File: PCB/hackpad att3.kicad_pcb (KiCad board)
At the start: 2 copper layers, 99 x 41 mm, 12 parts, among them SW1 SW_Push, SW2 SW_Push, SW3 SW_Push, SW4 SW_Push, SW5 SW_Push, SW6 SW_Push, SW9 RotaryEncoder_Switch, U1 XIAO-RP2040-DIP

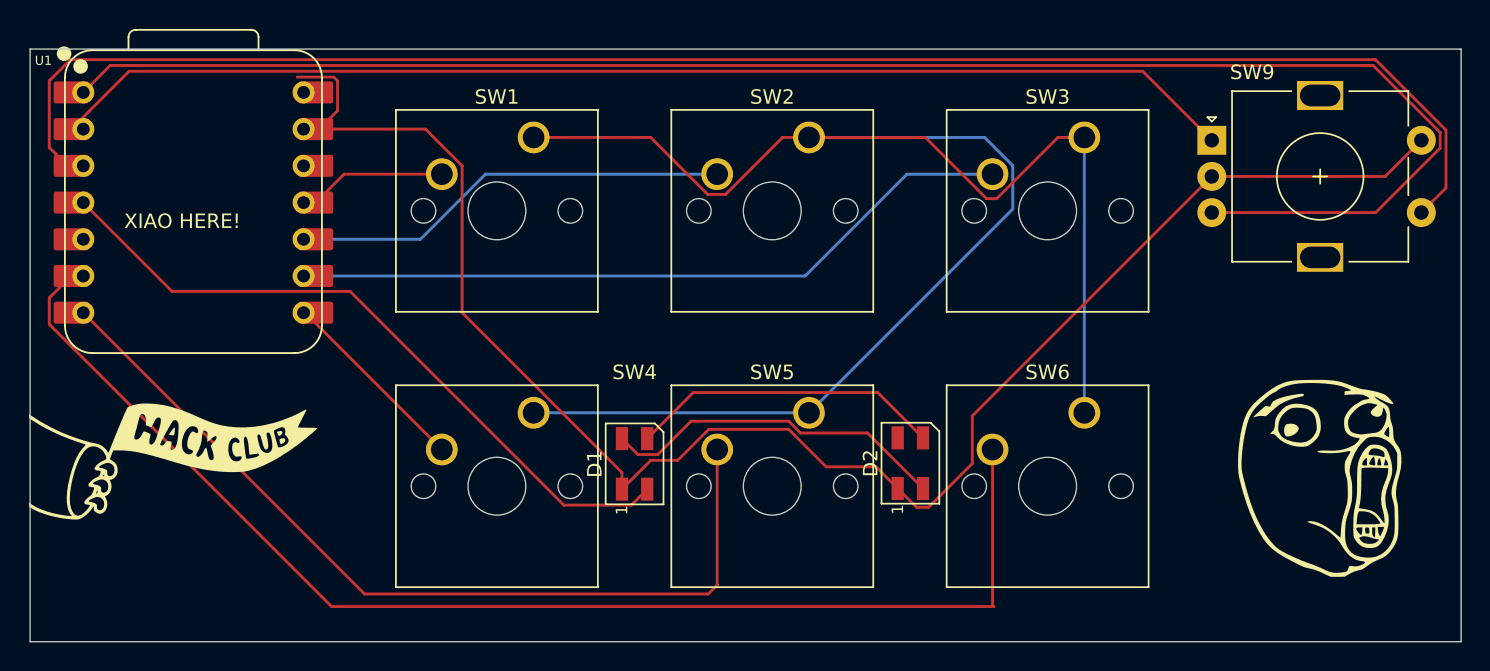
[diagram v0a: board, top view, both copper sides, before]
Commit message: Add PCB folder
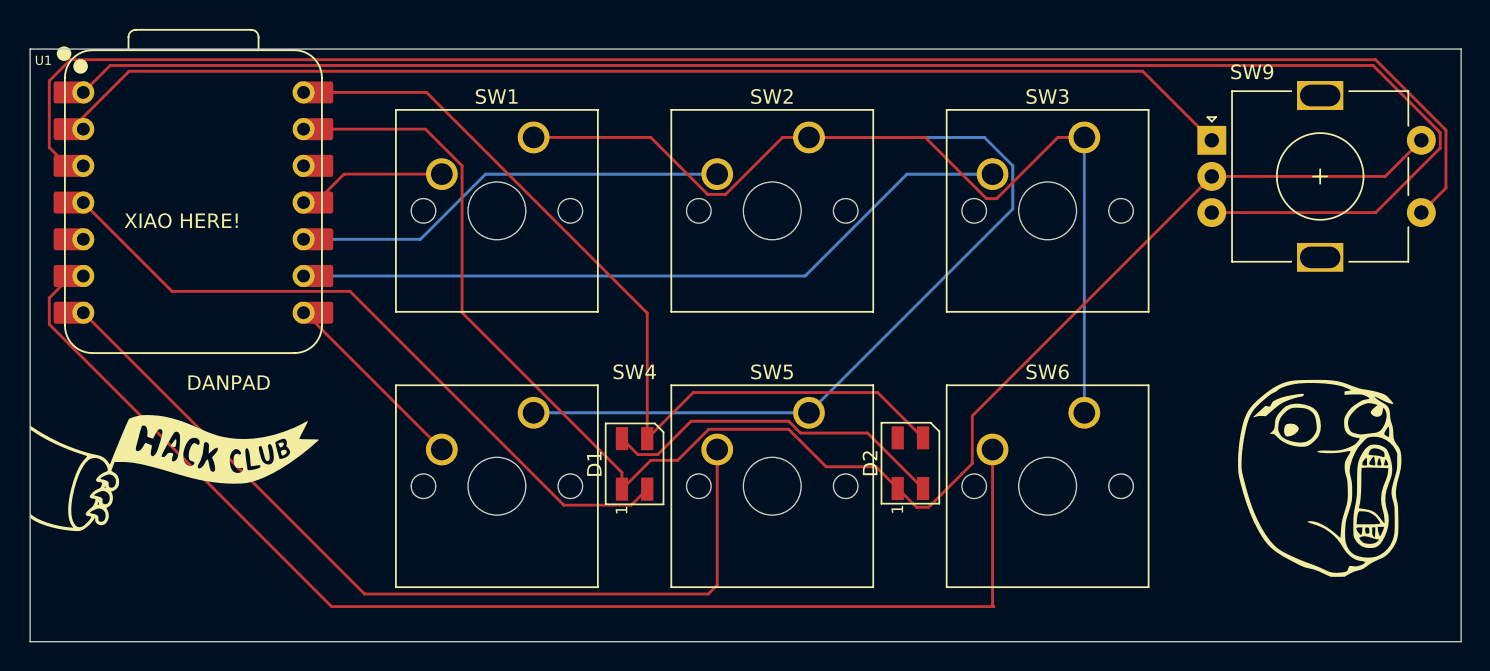
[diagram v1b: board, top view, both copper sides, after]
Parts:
- moved G*** 0.81 mm to (45.7, 44.3)
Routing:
- net +5V: track 22.1 -> 60.0 mm
- net GND: track 117.7 -> 110.9 mm
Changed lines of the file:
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@@
 	(footprint "LOGO"
 		(layer "F.Cu")
-		(at 45.6 43.5)
+		(at 45.7 44.3)
 		(property "Reference" "G***"
 			(at 0 0 0)
@@
 		(layer "Edge.Cuts")
 	)
+	(gr_text "DANPAD"
+		(at 46.5 38.7 0)
+		(layer "F.SilkS")
+		(effects
+			(font
+				(size 1 1)
+				(thickness 0.1)
+			)
+			(justify left bottom)
+		)
+	)
 	(gr_text "XIAO HERE!"
 		(at 42.18125 27.5 0)
@@
 		)
 	)
-	(gr_text "DANPAD"
-		(at 46.4 37.9 0)
-		(layer "Edge.Cuts")
-		(effects
-			(font
-				(size 1 1)
-				(thickness 0.15)
-			)
-			(justify left bottom)
-		)
-	)
 	(segment
 		(start 64.165 42.70375)
@@
 	)
 	(segment
-		(start 54.15969 16.937)
-		(end 56.690626 16.937)
-		(width 0.2)
-		(layer "F.Cu")
-		(net 2)
-	)
-	(segment
 		(start 97.005 46.7)
 		(end 97.84028 46.7)
@@
 	)
 	(segment
-		(start 56.952 19.26563)
-		(end 55.67763 20.54)
-		(width 0.2)
-		(layer "F.Cu")
-		(net 2)
-	)
-	(segment
 		(start 55.67763 20.54)
 		(end 54.6 20.54)
@@
 	)
 	(segment
-		(start 56.952 17.198374)
-		(end 56.952 19.26563)
-		(width 0.2)
-		(layer "F.Cu")
-		(net 2)
-	)
-	(segment
 		(start 76.625 44.292436)
 		(end 65.566 33.233436)
@@
 	)
 	(segment
-		(start 56.690626 16.937)
-		(end 56.952 17.198374)
-		(width 0.2)
-		(layer "F.Cu")
-		(net 2)
-	)
-	(segment
 		(start 76.625 45.45)
 		(end 78.623 43.452)
@@
 	)
 	(segment
+		(start 55.435 18)
+		(end 63.106066 18)
+		(width 0.2)
+		(layer "F.Cu")
+		(net 6)
+	)
+	(segment
+		(start 63.106066 18)
+		(end 78.375 33.268934)
+		(width 0.2)
+		(layer "F.Cu")
+		(net 6)
+	)
+	(segment
 		(start 97.455 41.9)
 		(end 94.31775 38.76275)
 		(width 0.2)
 		(layer "F.Cu")
+		(net 6)
+	)
+	(segment
+		(start 78.375 33.268934)
+		(end 78.375 41.95)
+		(width 0.2)
+		(layer "F.Cu")
